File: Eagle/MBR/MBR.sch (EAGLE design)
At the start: 39 parts

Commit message: finished most boards
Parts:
- added C1, C2, C3, C4: (no value), rcl:C-US025-024X044
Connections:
- removed net N$19: BOARD_CONNECTOR.20, CLOCK_GATE.2A, CLOCK_GATE.2B, CLOCK_GATE.3A, CLOCK_GATE.3B, CLOCK_GATE.4A, CLOCK_GATE.4B, CLOCK_GATE.GND, LED0.C, LED1.C, LED10.C, LED11.C, LED12.C, LED13.C, LED14.C, LED15.C, LED2.C, LED3.C, LED4.C, LED5.C, LED6.C, LED7.C, LED8.C, LED9.C, OUTPUT_0-7.GND, OUTPUT_8-15.GND, REGISTER_0-7.GND, REGISTER_0-7.~OE, REGISTER_8-15.GND, REGISTER_8-15.~OE
- removed net N$5: BOARD_CONNECTOR.19, CLOCK_GATE.VCC, OUTPUT_0-7.VCC, OUTPUT_8-15.VCC, REGISTER_0-7.VCC, REGISTER_8-15.VCC
- new net GND: BOARD_CONNECTOR.20, C1.1, C2.1, C3.1, C4.1, CLOCK_GATE.2A, CLOCK_GATE.2B, CLOCK_GATE.3A, CLOCK_GATE.3B, CLOCK_GATE.4A, CLOCK_GATE.4B, CLOCK_GATE.GND, LED0.C, LED1.C, LED10.C, LED11.C, LED12.C, LED13.C, LED14.C, LED15.C, LED2.C, LED3.C, LED4.C, LED5.C, LED6.C, LED7.C, LED8.C, LED9.C, OUTPUT_0-7.GND, OUTPUT_8-15.GND, REGISTER_0-7.GND, REGISTER_0-7.~OE, REGISTER_8-15.GND, REGISTER_8-15.~OE
- new net VCC: BOARD_CONNECTOR.19, C1.2, C2.2, C3.2, C4.2, CLOCK_GATE.VCC, OUTPUT_0-7.VCC, OUTPUT_8-15.VCC, REGISTER_0-7.VCC, REGISTER_8-15.VCC

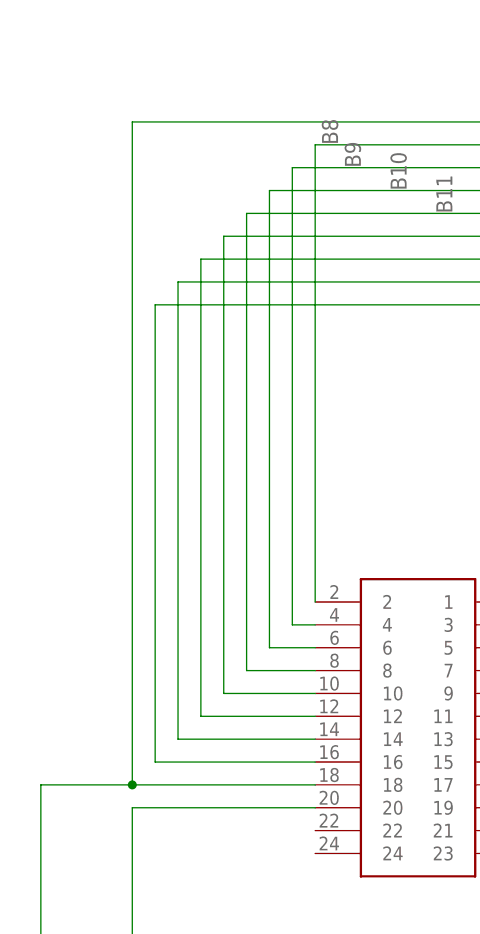
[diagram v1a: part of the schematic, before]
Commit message: added Clock
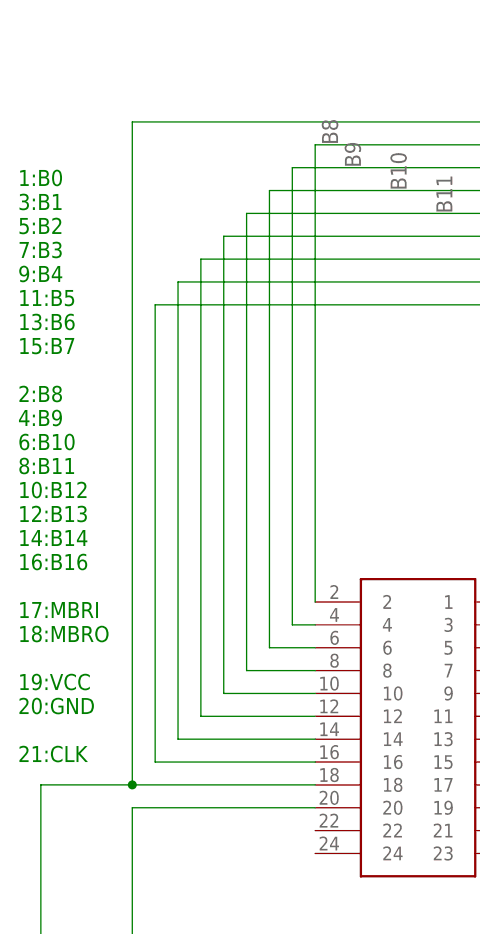
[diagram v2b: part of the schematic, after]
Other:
- note added: "1:B0 3:B1 5:B2 7:B3 9:B4 11:B5 13:B6 15:B7 2:B8 4:B9 6:B10 8:B11 10:B12 12:B13 14:B14 16:B16 17:MBRI 18:MBRO 19:VCC 20:GND 21:CLK"
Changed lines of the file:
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@@
 <sheet>
 <plain>
+<text x="-78.74" y="73.66" size="1.778" layer="91">1:B0
+3:B1
+5:B2
+7:B3
+9:B4
+11:B5
+13:B6
+15:B7
+2:B8
+4:B9
+6:B10
+8:B11
+10:B12
+12:B13
+14:B14
+16:B16
+17:MBRI
+18:MBRO
+19:VCC
+20:GND
+21:CLK</text>
 </plain>
 <instances>
@@
 </drawing>
 <compatibility>
+<note version="6.3" minversion="6.2.2" severity="warning">
+Since Version 6.2.2 text objects can contain more than one line,
+which will not be processed correctly with this version.
+</note>
 <note version="8.2" severity="warning">
 Since Version 8.2, EAGLE supports online libraries. The ids
